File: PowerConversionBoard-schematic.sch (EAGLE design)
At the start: 59 parts, among them Q1 MOSFET_PCH-NDS8434, Q2 MOSFET_PCH-NDS8434, U3 AZ1117EH-3.3TRG1

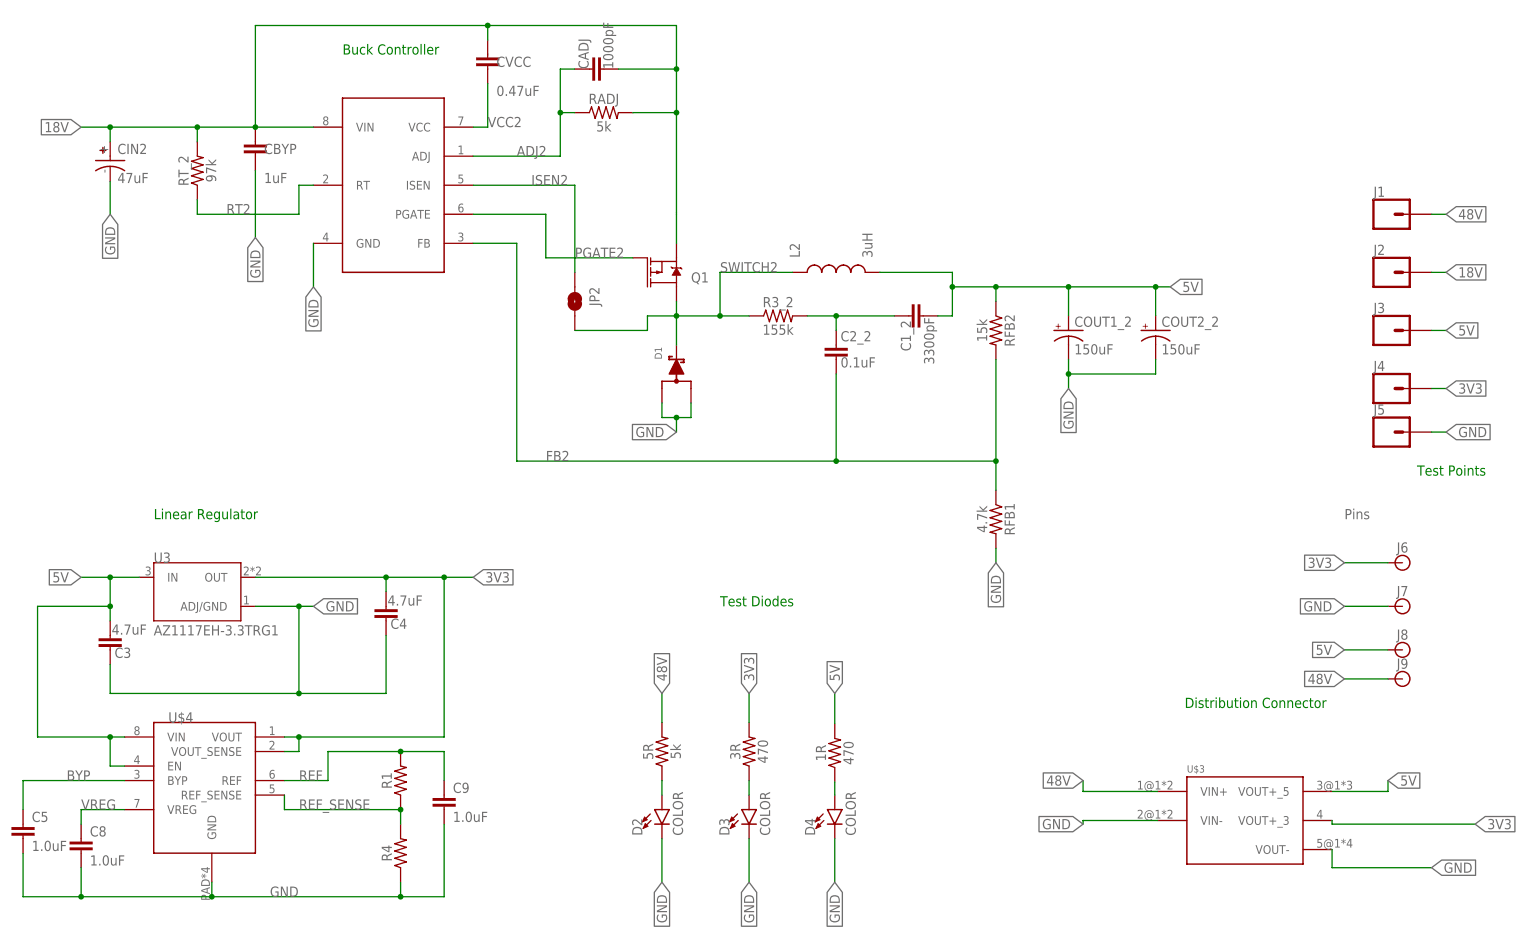
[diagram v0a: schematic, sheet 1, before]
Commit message: V3 with buck converter of previous years
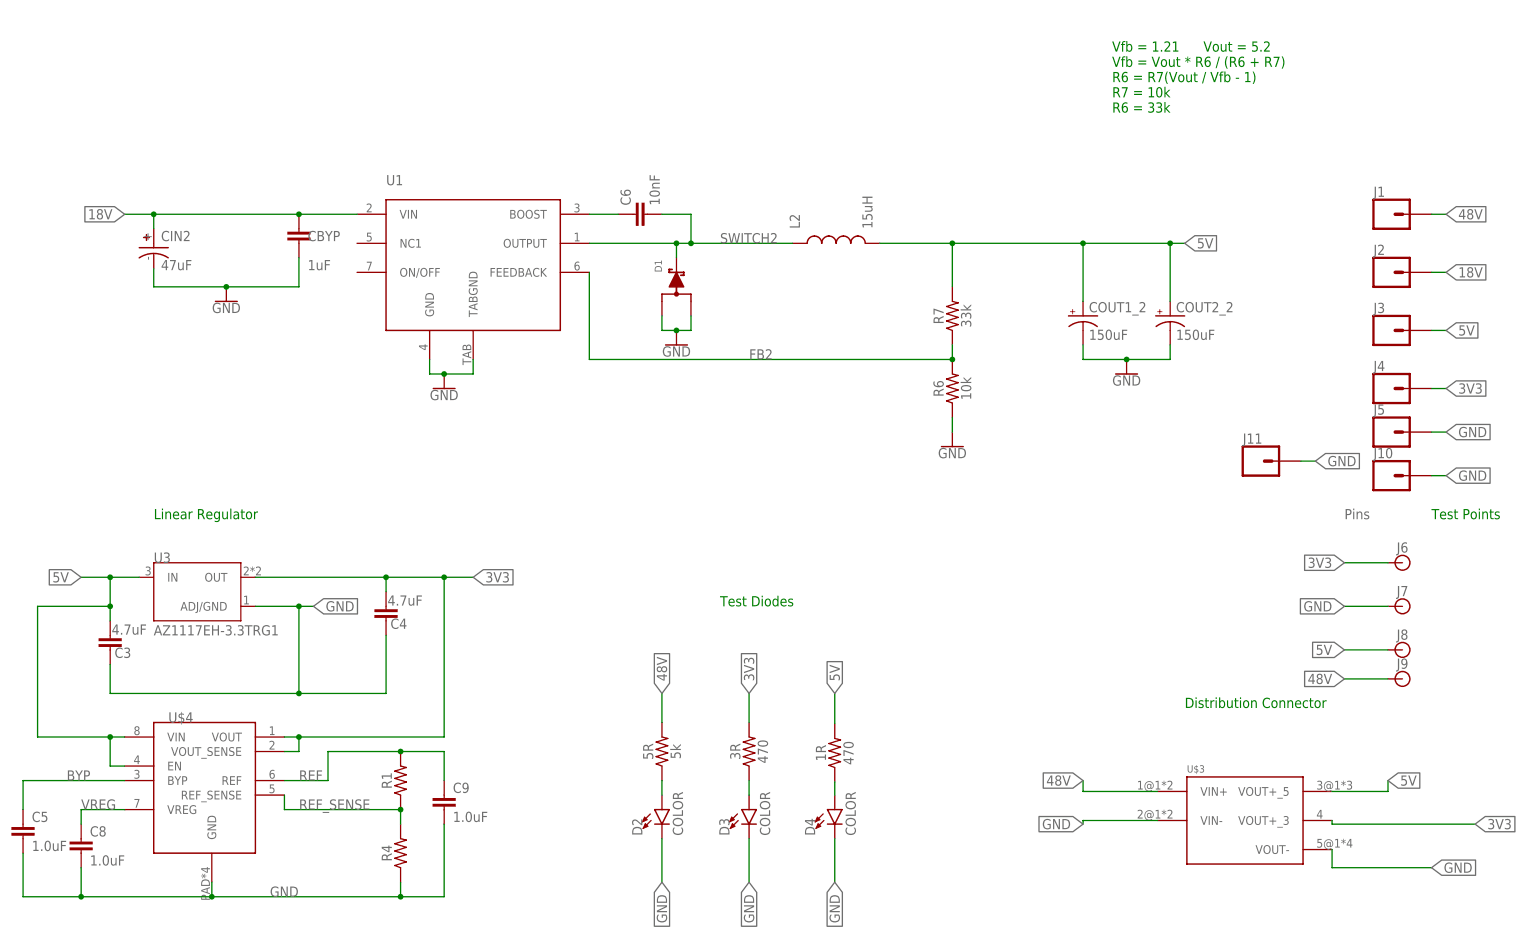
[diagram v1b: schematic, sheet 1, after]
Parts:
- removed C1_1, C1_2: 3300pF, SparkFun-Capacitors:12PF-0603-50V-5%
- removed C2_1, C2_2: 0.1uF, SparkFun-Capacitors:12PF-0603-50V-5%
- removed CADJ, CADJ1: 1000pF, SparkFun-Capacitors:5.6PF-0603-50V-5%
- removed CVCC, CVCC1: 0.47uF, SparkFun-Capacitors:5.6PF-0603-50V-5%
- removed JP1, JP2: JUMPER-SMT_2_NO_SILK, SparkFun-Jumpers:JUMPER-SMT_2_NO_SILK
- removed Q1, Q2: MOSFET_PCH-NDS8434, SparkFun-DiscreteSemi:MOSFET_PCH-NDS8434
- removed R2_1: 400k, SparkFun-Resistors:RESISTOR0603
- removed R3_2: 155k, SparkFun-Resistors:RESISTOR0603
- removed RADJ: 5k, SparkFun-Resistors:RESISTOR0603
- removed RADJ1: 1.8k, SparkFun-Resistors:RESISTOR0603
- removed RFB1: 4.7k, SparkFun-Resistors:RESISTOR0603
- removed RFB2: 15k, SparkFun-Resistors:RESISTOR0603
- removed RT1: 366k, SparkFun-Resistors:82OHM-0603-1/10W-1%
- removed RT_2: 97k, SparkFun-Resistors:82OHM-0603-1/10W-1%
- removed U$1, U$2: LM5085, Buck_Controller:LM5085
- added C6: 10nF, SparkFun-Capacitors:10NF-0603-50V-10%
- added CBS: 0.1uF, SparkFun-Capacitors:3.3NF-0603-100V-10%
- added D6: SWITCHMODE_SCHOTTKY, Schottky Diode 8A - MBRD835LT4G:SWITCHMODE_SCHOTTKY
- added J10, J11, J12: (no value), SparkFun-Connectors:CONN_01
- added R6: 10k, SparkFun-Resistors:10KOHM-0603-1/10W-1%
- added R7: 33k, SparkFun-Resistors:33KOHM-0603-1/10W-1%
- added RT: 49.9k, SparkFun-Resistors:RESISTOR0603
- added U1: LM2678, IC, Buck Controller - LM2678, LM2576:LM2678
- added U4: (no value), IC, Buck Controller - LM2678, LM2576:LMR16020
- L1: value 18uH -> 47uH
- L2: value 3uH -> 15uH
- RFB1_1: value 5.6k -> 10k
- RFB2_1: value 75k -> 230k
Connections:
- removed net ADJ1: CADJ1.1, RADJ1.1, U$2.ADJ
- removed net ADJ2: CADJ.1, RADJ.1, U$1.ADJ
- removed net ISEN1: JP1.2, U$2.ISEN
- removed net ISEN2: JP2.1, U$1.ISEN
- removed net N$1: C1_1.2, C2_1.1, R2_1.2
- removed net N$11: C1_2.2, C2_2.1, R3_2.2
- removed net PGATE1: Q2.G, U$2.PGATE
- removed net PGATE2: Q1.G, U$1.PGATE
- removed net RT1: RT1.1, U$2.RT
- removed net RT2: RT_2.1, U$1.RT
- removed net VCC1: CVCC1.2, U$2.VCC
- removed net VCC2: CVCC.2, U$1.VCC
- new net 18V_EXT: D6.A@1, D6.A@2, J12.1
- new net BOOTSTRAP: CBS.1, U4.BOOT
- new net BST: C6.1, U1.BOOST
- new net RT: RT.1, U4.RT/SYNC
- net 18V: now also D6.C, U1.VIN; no longer C1_1.1, CADJ.2, CVCC.1, Q1.S, RADJ.2, RT_2.2, U$1.VIN
- net 48V: now also U4.EN, U4.VIN; no longer CADJ1.2, CVCC1.1, Q2.S, RADJ1.2, RT1.2, U$2.VIN
- net 5V: now also R7.2; no longer C1_2.1, RFB2.1
- net FB1: now also U4.FB; no longer C2_1.2, U$2.FB
- net FB2: now also R6.2, R7.1, U1.FEEDBACK; no longer C2_2.2, RFB1.1, RFB2.2, U$1.FB
- net GND: now also J10.1, J11.1, R6.1, RT.2, U1.GND, U1.TABGND, U4.GND; no longer RFB1.2, U$1.GND, U$2.GND
- net SWITCH1: now also CBS.2, U4.SW; no longer JP1.1, Q2.D, R2_1.1
- net SWITCH2: now also C6.2, U1.OUTPUT; no longer JP2.2, Q1.D, R3_2.1
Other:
- note added: "Vfb = 1.21 Vout = 5.2 Vfb = Vout * R6 / (R6 + R7) R6 = R7(Vout / Vfb - 1) R7 = 10k R6 = 33k"
- note removed: "Buck Controller"
- moved on the sheet: CBYP, CIN2, COUT1_2, COUT2_2, D1, D5, L1, L2, RFB1_1, RFB2_1
